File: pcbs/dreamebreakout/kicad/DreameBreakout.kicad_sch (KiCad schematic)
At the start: 9 parts, among them J1.1 To Robot SoC, J1.2 To Robot MCU, J2 SoC Breakout, J3 MCU Breakout, J4 SoC_FEL_USB, J5 OTG_USB, SW1 SoC_Boot_SEL_BTN

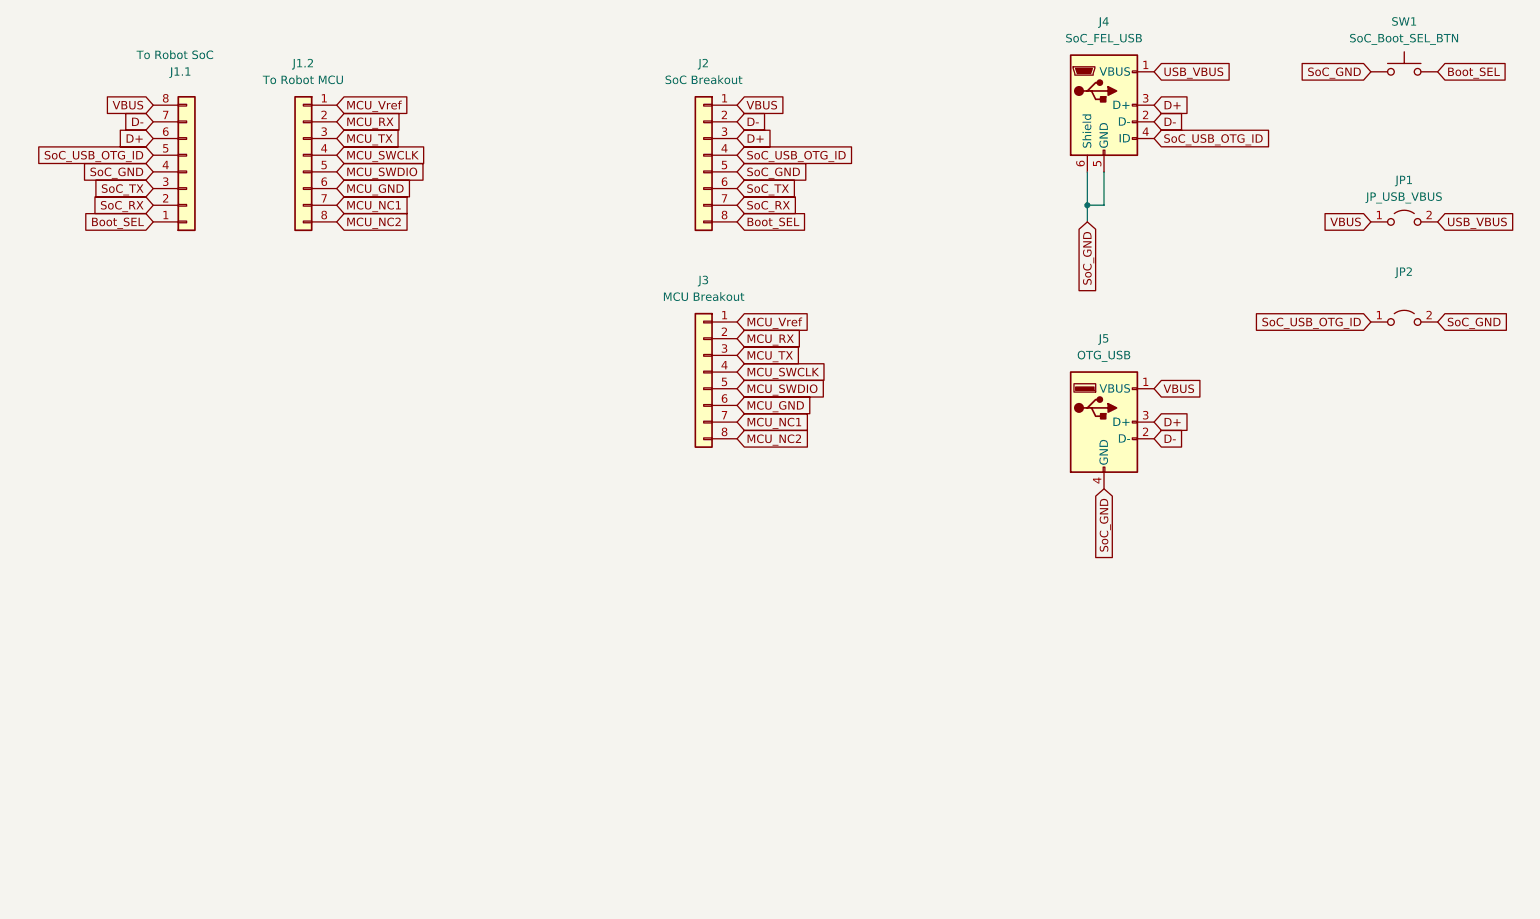
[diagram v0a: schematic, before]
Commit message: Update original Dreame breakout board
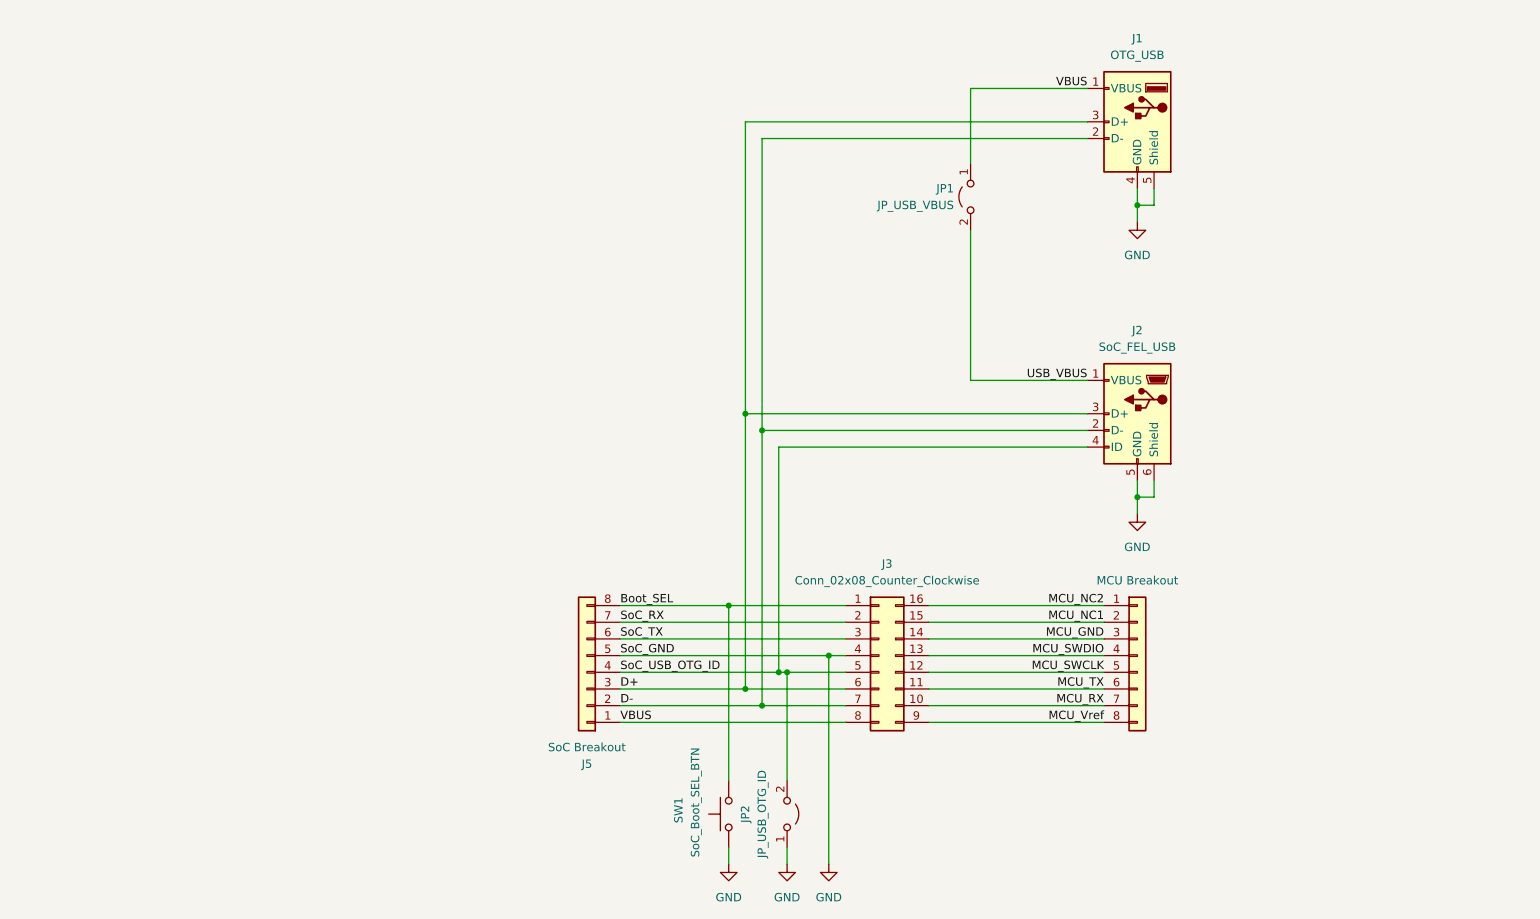
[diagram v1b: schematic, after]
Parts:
- removed J1.1: To Robot SoC, Custom:DGI_8_SMDPADS, symbol Connector_Generic:Conn_01x08
- removed J1.2: To Robot MCU, Custom:DGI_8_SMDPADS, symbol Connector_Generic:Conn_01x08
- removed J5: OTG_USB, Custom:ONSHORE_USB-A1VSB6, symbol Connector:USB_A
- added J1: OTG_USB, Custom:ONSHORE_USB-A1VSB6, symbol Connector:USB_A
- added J3: Conn_02x08_Counter_Clockwise, Dreame:Connector 02x08 2.00mm Edge Mount, symbol Connector_Generic:Conn_02x08_Counter_Clockwise
- JP1: footprint Connector_PinSocket_2.00mm:PinSocket_1x02_P2.00mm_Vertical -> Connector_PinHeader_2.54mm:PinHeader_1x02_P2.54mm_Vertical
- JP2: value (none) -> JP_USB_OTG_ID; footprint (none) -> Connector_PinHeader_2.54mm:PinHeader_1x02_P2.54mm_Vertical
- renumbered J4 to J2, J3 to J4, J2 to J5
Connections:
- net Boot_SEL: now also J3.1 (Pin_1)
- net D+: now also J1.3 (D+), J3.6 (Pin_6)
- net D-: now also J1.2 (D-), J3.7 (Pin_7)
- net MCU_GND: now also J4.3 (Pin_3), J3.14 (Pin_14); no longer J4.6 (Pin_6)
- net MCU_NC1: now also J4.2 (Pin_2), J3.15 (Pin_15); no longer J4.7 (Pin_7)
- net MCU_NC2: now also J4.1 (Pin_1), J3.16 (Pin_16); no longer J4.8 (Pin_8)
- net MCU_RX: now also J4.7 (Pin_7), J3.10 (Pin_10); no longer J4.2 (Pin_2)
- net MCU_SWCLK: now also J4.5 (Pin_5), J3.12 (Pin_12); no longer J4.4 (Pin_4)
- net MCU_SWDIO: now also J4.4 (Pin_4), J3.13 (Pin_13); no longer J4.5 (Pin_5)
- net MCU_TX: now also J4.6 (Pin_6), J3.11 (Pin_11); no longer J4.3 (Pin_3)
- net MCU_Vref: now also J4.8 (Pin_8), J3.9 (Pin_9); no longer J4.1 (Pin_1)
- net SoC_RX: now also J3.2 (Pin_2)
- net SoC_TX: now also J3.3 (Pin_3)
- net SoC_USB_OTG_ID: now also JP2.2 (B), J3.5 (Pin_5); no longer JP2.1 (A)
- net VBUS: now also J1.1 (VBUS), J3.8 (Pin_8)
- net SoC_GND renamed GND
- net GND: now also JP2.1 (A), J1.4 (GND), J1.5 (Shield), J3.4 (Pin_4); no longer JP2.2 (B)
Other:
- company: (none) -> Alexander Knapik
- title: (none) -> Dreame Breakout Original
- moved on the sheet: J2, J5, JP1, JP2, SW1
